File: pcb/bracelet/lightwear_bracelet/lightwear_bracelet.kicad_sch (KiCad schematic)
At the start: 20 parts, among them Q1 NMOS, SW1 SW_SPST, U1 ATtiny1616-M, U2 TP4054

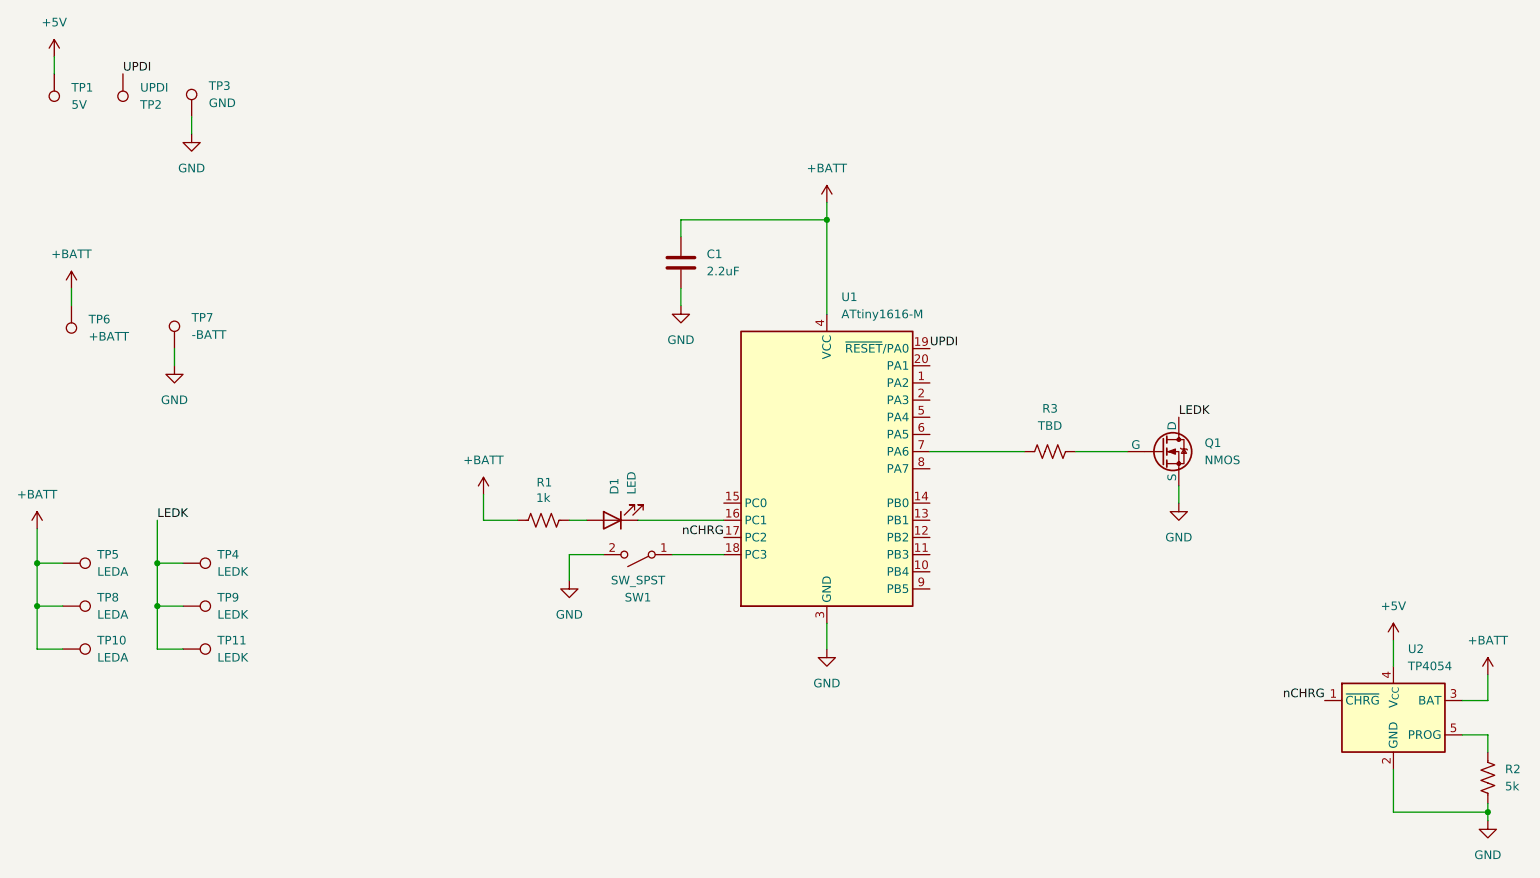
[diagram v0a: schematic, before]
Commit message: 15x20mm battery version done
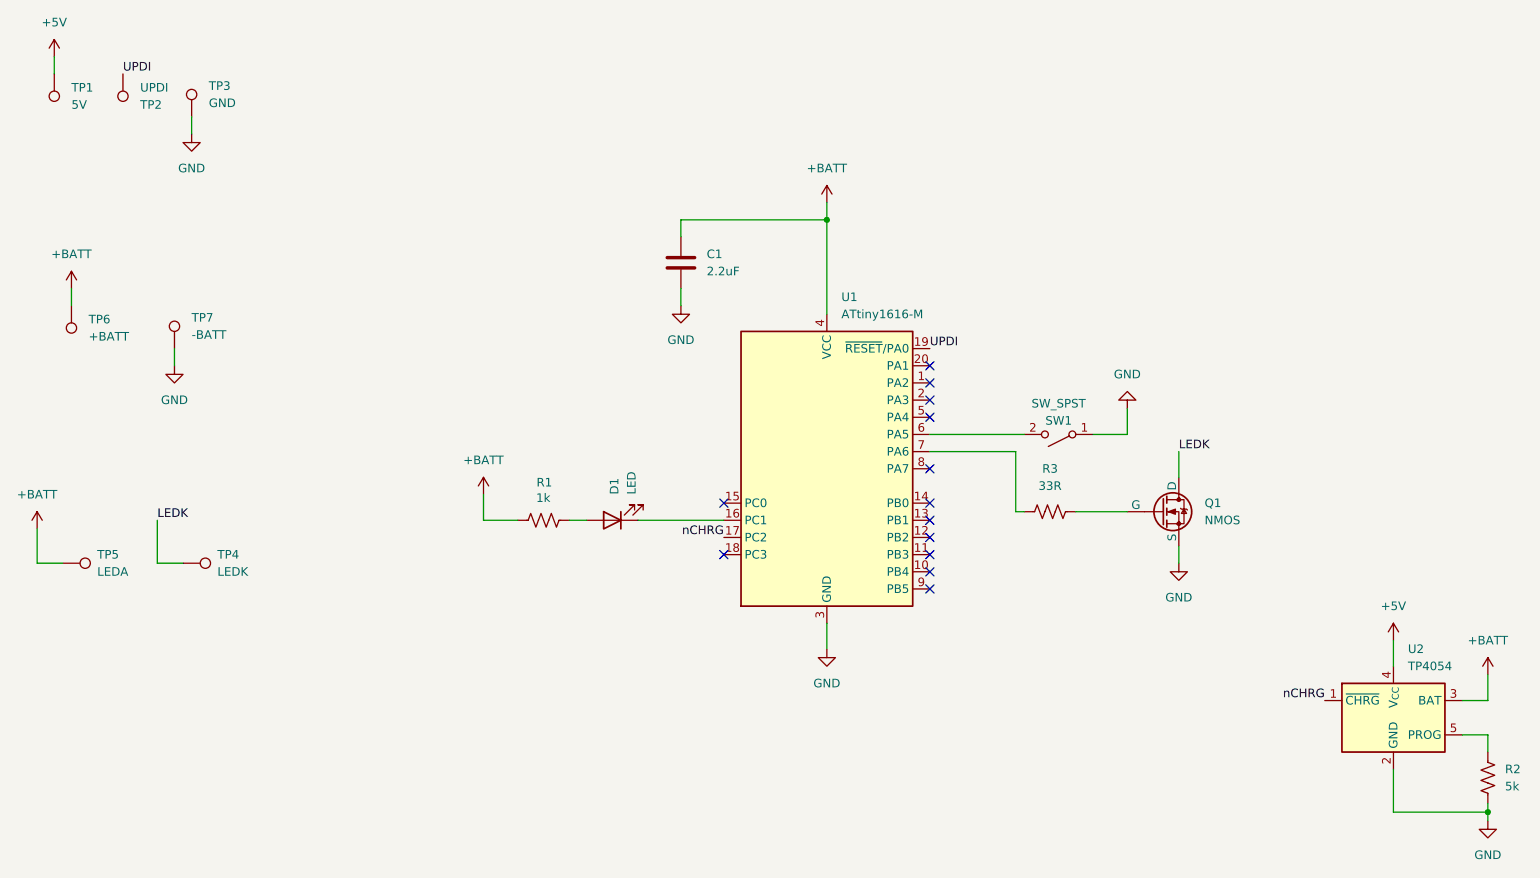
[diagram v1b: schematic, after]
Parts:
- removed TP10, TP8: LEDA, footprints:TestPoint_Pad_4.0x1.4mm, symbol Connector:TestPoint
- removed TP11, TP9: LEDK, footprints:TestPoint_Pad_4.0x1.4mm, symbol Connector:TestPoint
- D1: footprint LED_SMD:LED_0201_0603Metric -> LED_SMD:LED_0603_1608Metric
- Q1: footprint Package_TO_SOT_SMD:SOT-23 -> footprints:SOT-23-MOSFET
- R2: footprint Resistor_SMD:R_0402_1005Metric -> LED_SMD:LED_0402_1005Metric_Pad0.77x0.64mm_HandSolder
- R3: value TBD -> 33R
- SW1: footprint footprints:SW4_PTS815 SJM 250 SMTR LFS_CNK -> footprints:SMT_231GPLFS
- TP1, TP2, TP3: footprint TestPoint:TestPoint_Pad_D1.5mm -> footprints:TestPoint_Pad_5.0x2mm_slim
- TP4, TP5: footprint footprints:TestPoint_Pad_4.0x1.4mm -> footprints:TestPoint_Pad_2.0x1.5mm_slim
- TP6, TP7: footprint footprints:TestPoint_Pad_2.0x2.0mm_slim -> footprints:TestPoint_Pad_2.0x1.2mm_slim
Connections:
- net GND: now also SW1.1 (A); no longer SW1.2 (B)
- net at U1.18 (PC3): no longer SW1.1 (A)
- net at U1.6 (PA5): now also SW1.2 (B)
- no-connect marks 0 -> 13
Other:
- moved on the sheet: Q1, R3, SW1

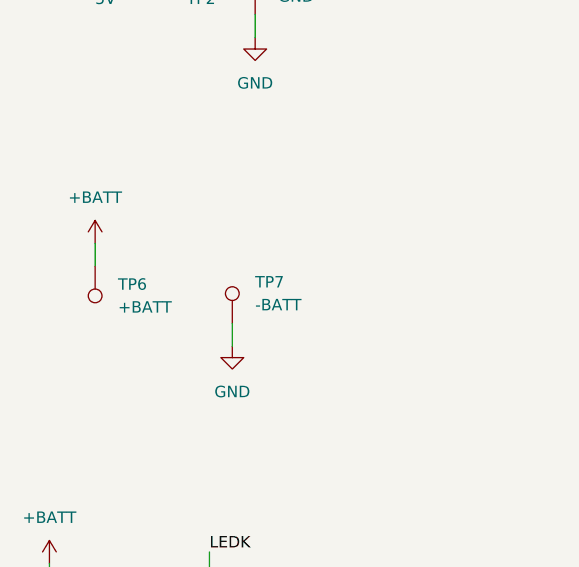
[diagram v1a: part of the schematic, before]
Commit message: code for bracelet working. 4 brightness modes (including OFF) and battery checking (25% increments)
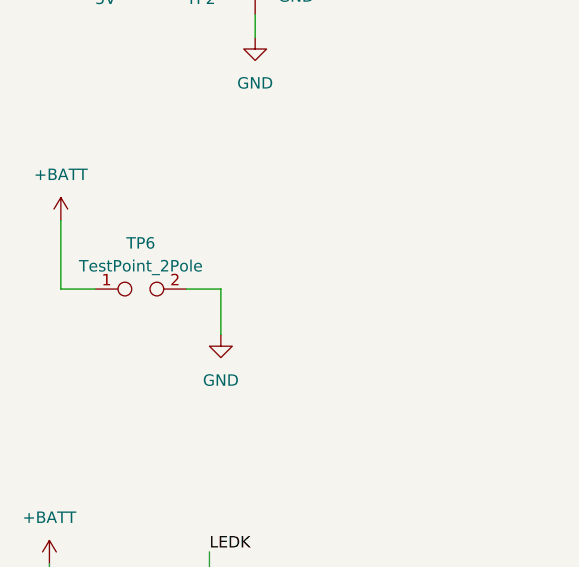
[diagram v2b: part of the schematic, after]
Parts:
- removed TP6: +BATT, footprints:TestPoint_Pad_2.0x1.2mm_slim, symbol Connector:TestPoint
- removed TP7: -BATT, footprints:TestPoint_Pad_2.0x1.2mm_slim, symbol Connector:TestPoint
- added TP6: TestPoint_2Pole, footprints:BatteryBMSBoardPads, symbol Connector:TestPoint_2Pole
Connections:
- net +BATT: now also TP6.1
- net GND: now also TP6.2
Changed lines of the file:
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@@
+	(wire
+		(pts
+			(xy 30.48 63.5) (xy 30.48 71.12)
+		)
+		(stroke
+			(width 0)
+			(type default)
+		)
+	)
 	(wire
 		(pts
@@
 	(wire
 		(pts
+			(xy 44.45 71.12) (xy 48.26 71.12)
+		)
+		(stroke
+			(width 0)
+			(type default)
+		)
+	)
+	(wire
+		(pts
 			(xy 198.12 106.68) (xy 198.12 104.14)
 		)
@@
 	(wire
 		(pts
-			(xy 49.53 74.93) (xy 49.53 77.47)
-		)
-		(stroke
-			(width 0)
-			(type default)
-		)
-	)
-	(wire
-		(pts
 			(xy 182.88 99.06) (xy 190.5 99.06)
 		)
@@
 	(wire
 		(pts
-			(xy 34.29 66.04) (xy 34.29 68.58)
-		)
-		(stroke
-			(width 0)
-			(type default)
-		)
-	)
-	(wire
-		(pts
 			(xy 229.87 143.51) (xy 243.84 143.51)
 		)
@@
 	(wire
 		(pts
+			(xy 34.29 71.12) (xy 30.48 71.12)
+		)
+		(stroke
+			(width 0)
+			(type default)
+		)
+	)
+	(wire
+		(pts
 			(xy 240.03 132.08) (xy 243.84 132.08)
 		)
@@
 		(pts
 			(xy 243.84 143.51) (xy 243.84 144.78)
+		)
+		(stroke
+			(width 0)
+			(type default)
+		)
+	)
+	(wire
+		(pts
+			(xy 48.26 71.12) (xy 48.26 76.2)
 		)
 		(stroke
@@
 	(symbol
 		(lib_id "power:GND")
-		(at 49.53 77.47 0)
+		(at 48.26 76.2 0)
 		(unit 1)
 		(exclude_from_sim no)
@@
 		(fields_autoplaced yes)
 		(property "Reference" "#PWR04"
-			(at 49.53 83.82 0)
+			(at 48.26 82.55 0)
 			(effects
 				(font
@@
 		)
 		(property "Value" "GND"
-			(at 49.53 82.55 0)
+			(at 48.26 81.28 0)
 			(effects
 				(font
@@
 		)
 		(property "Footprint" ""
-			(at 49.53 77.47 0)
+			(at 48.26 76.2 0)
 			(effects
 				(font
@@
 		)
 		(property "Datasheet" ""
-			(at 49.53 77.47 0)
+			(at 48.26 76.2 0)
 			(effects
 				(font
@@
 		)
 		(property "Description" "Power symbol creates a global label with name \"GND\" , ground"
-			(at 49.53 77.47 0)
+			(at 48.26 76.2 0)
 			(effects
 				(font
@@
 	)
 	(symbol
+		(lib_id "Connector:TestPoint_2Pole")
+		(at 39.37 71.12 0)
+		(unit 1)
+		(exclude_from_sim no)
+		(in_bom yes)
+		(on_board yes)
+		(dnp no)
+		(fields_autoplaced yes)
+		(property "Reference" "TP6"
+			(at 39.37 66.04 0)
+			(effects
+				(font
+					(size 1.27 1.27)
+				)
+			)
+		)
+		(property "Value" "TestPoint_2Pole"
+			(at 39.37 68.58 0)
+			(effects
+				(font
+					(size 1.27 1.27)
+				)
+			)
+		)
+		(property "Footprint" "footprints:BatteryBMSBoardPads"
+			(at 39.37 71.12 0)
+			(effects
+				(font
+					(size 1.27 1.27)
+				)
+				(hide yes)
+			)
+		)
+		(property "Datasheet" "~"
+			(at 39.37 71.12 0)
+			(effects
+				(font
+					(size 1.27 1.27)
+				)
+				(hide yes)
+			)
+		)
+		(property "Description" "2-polar test point"
+			(at 39.37 71.12 0)
+			(effects
+				(font
+					(size 1.27 1.27)
+				)
+				(hide yes)
+			)
+		)
+		(pin "1"
+		)
+		(pin "2"
+		)
+		(instances
+			(project ""
+				(path "/a0570445-ed22-48e6-80a6-1819b94aba45"
+					(reference "TP6")
+					(unit 1)
+				)
+			)
+		)
+	)
+	(symbol
 		(lib_id "Connector:TestPoint")
 		(at 50.8 106.68 270)
@@
 	(symbol
 		(lib_id "Connector:TestPoint")
-		(at 49.53 74.93 0)
-		(unit 1)
-		(exclude_from_sim no)
-		(in_bom yes)
-		(on_board yes)
-		(dnp no)
-		(fields_autoplaced yes)
-		(property "Reference" "TP7"
-			(at 52.07 70.3579 0)
-			(effects
-				(font
-					(size 1.27 1.27)
-				)
-				(justify left)
-			)
-		)
-		(property "Value" "-BATT"
-			(at 52.07 72.8979 0)
-			(effects
-				(font
-					(size 1.27 1.27)
-				)
-				(justify left)
-			)
-		)
-		(property "Footprint" "footprints:TestPoint_Pad_2.0x1.2mm_slim"
-			(at 54.61 74.93 0)
-			(effects
-				(font
-					(size 1.27 1.27)
-				)
-				(hide yes)
-			)
-		)
-		(property "Datasheet" "~"
-			(at 54.61 74.93 0)
-			(effects
-				(font
-					(size 1.27 1.27)
-				)
-				(hide yes)
-			)
-		)
-		(property "Description" "test point"
-			(at 49.53 74.93 0)
-			(effects
-				(font
-					(size 1.27 1.27)
-				)
-				(hide yes)
-			)
-		)
-		(pin "1"
-		)
-		(instances
-			(project "lightwear_bracelet"
-				(path "/a0570445-ed22-48e6-80a6-1819b94aba45"
-					(reference "TP7")
-					(unit 1)
-				)
-			)
-		)
-	)
-	(symbol
-		(lib_id "Connector:TestPoint")
 		(at 41.91 34.29 0)
 		(mirror x)
@@
 	(symbol
 		(lib_id "Connector:TestPoint")
-		(at 34.29 68.58 180)
-		(unit 1)
-		(exclude_from_sim no)
-		(in_bom yes)
-		(on_board yes)
-		(dnp no)
-		(fields_autoplaced yes)
-		(property "Reference" "TP6"
-			(at 36.83 70.6119 0)
-			(effects
-				(font
-					(size 1.27 1.27)
-				)
-				(justify right)
-			)
-		)
-		(property "Value" "+BATT"
-			(at 36.83 73.1519 0)
-			(effects
-				(font
-					(size 1.27 1.27)
-				)
-				(justify right)
-			)
-		)
-		(property "Footprint" "footprints:TestPoint_Pad_2.0x1.2mm_slim"
-			(at 29.21 68.58 0)
-			(effects
-				(font
-					(size 1.27 1.27)
-				)
-				(hide yes)
-			)
-		)
-		(property "Datasheet" "~"
-			(at 29.21 68.58 0)
-			(effects
-				(font
-					(size 1.27 1.27)
-				)
-				(hide yes)
-			)
-		)
-		(property "Description" "test point"
-			(at 34.29 68.58 0)
-			(effects
-				(font
-					(size 1.27 1.27)
-				)
-				(hide yes)
-			)
-		)
-		(pin "1"
-		)
-		(instances
-			(project "lightwear_bracelet"
-				(path "/a0570445-ed22-48e6-80a6-1819b94aba45"
-					(reference "TP6")
-					(unit 1)
-				)
-			)
-		)
-	)
-	(symbol
-		(lib_id "Connector:TestPoint")
 		(at 31.75 34.29 180)
 		(unit 1)
@@
 	(symbol
 		(lib_id "power:+BATT")
-		(at 34.29 66.04 0)
+		(at 30.48 63.5 0)
 		(unit 1)
 		(exclude_from_sim no)
@@
 		(fields_autoplaced yes)
 		(property "Reference" "#PWR03"
-			(at 34.29 69.85 0)
+			(at 30.48 67.31 0)
 			(effects
 				(font
@@
 		)
 		(property "Value" "+BATT"
-			(at 34.29 60.96 0)
+			(at 30.48 58.42 0)
 			(effects
 				(font
@@
 		)
 		(property "Footprint" ""
-			(at 34.29 66.04 0)
+			(at 30.48 63.5 0)
 			(effects
 				(font
@@
 		)
 		(property "Datasheet" ""
-			(at 34.29 66.04 0)
+			(at 30.48 63.5 0)
 			(effects
 				(font
@@
 		)
 		(property "Description" "Power symbol creates a global label with name \"+BATT\""
-			(at 34.29 66.04 0)
-			(effects
-				(font
+			(at 30.48 63.5 0)
+			(effects
+				(font
